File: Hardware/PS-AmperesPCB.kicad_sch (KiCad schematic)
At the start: 10 parts, among them J1 PeripheralCAN, J2 PeripheralCAN

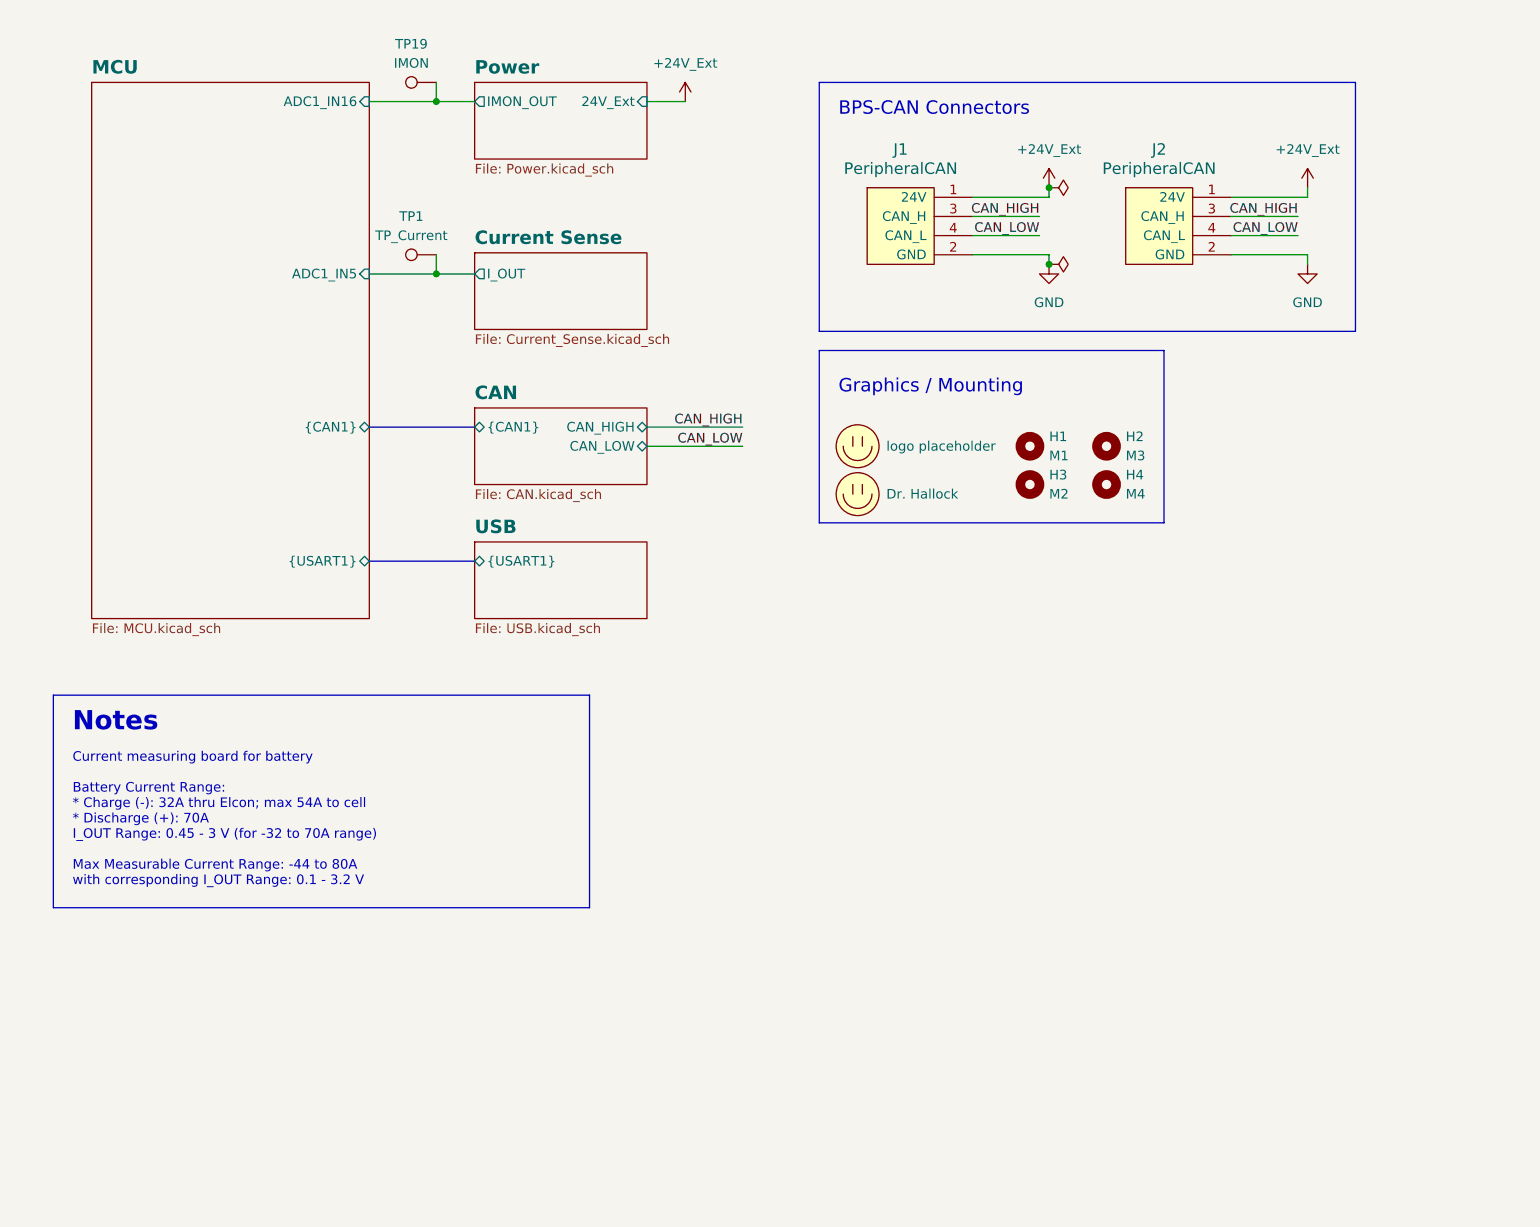
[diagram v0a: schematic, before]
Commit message: added documentation for current range; added VBUS led
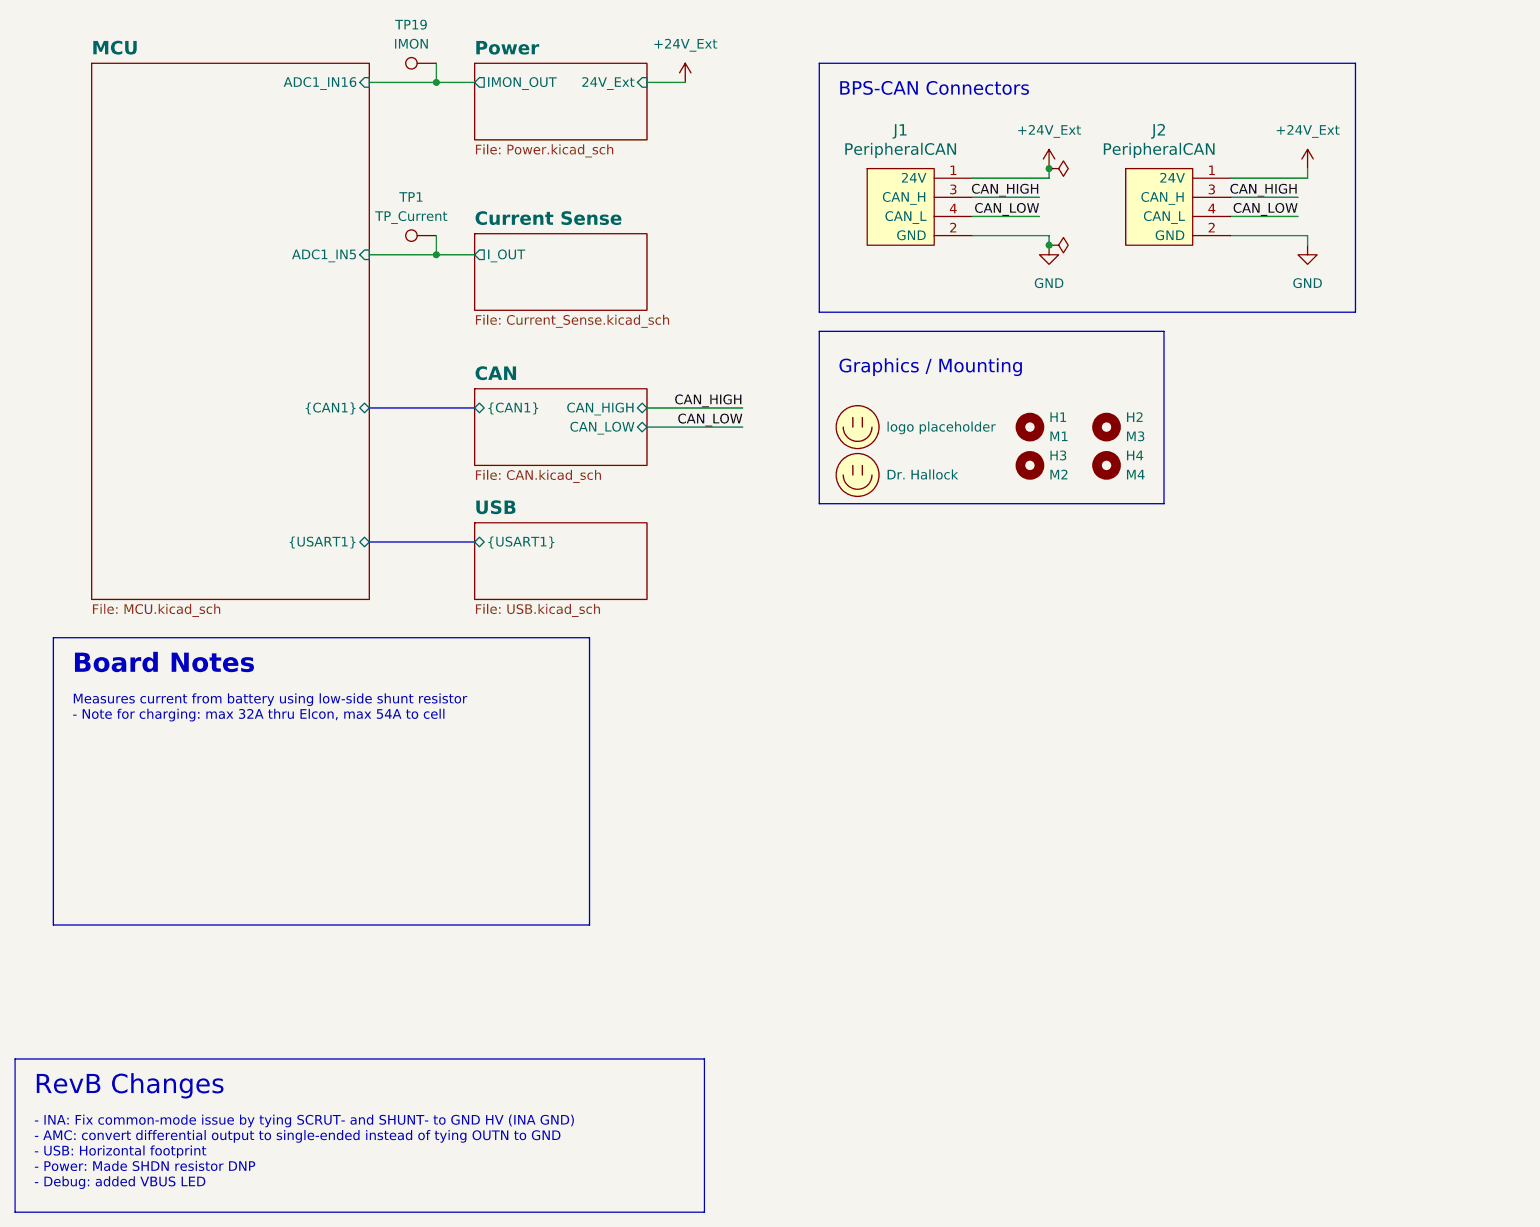
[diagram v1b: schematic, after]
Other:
- note added: "- INA: Fix common-mode issue by tying SCRUT- and SHUNT- to GND HV (INA GND) - AMC: convert differential output to single-ended instead of tying OUTN to GND - USB: Horizontal footprint - Power: Made SHDN resistor DNP - Debug: added VBUS LED"
- note added: "Board Notes"
- note added: "Measures current from battery using low-side shunt resistor - Note for charging: max 32A thru Elcon, max 54A to cell"
- note added: "RevB Changes"
- note removed: "Current measuring board for battery Battery Current Range: * Charge (-): 32A thru Elcon; max 54A to cell * Discharge (+): 70A I_OUT Range: 0.45 - 3 V (for -32 to 70A range) Max Measurable Current Range: -44 to 80A with corresponding I_OUT Range: 0.1 - 3.2 V"
- note removed: "Notes"
- moved on the sheet: H1, H2, H3, H4, J1, J2, TP1, TP19

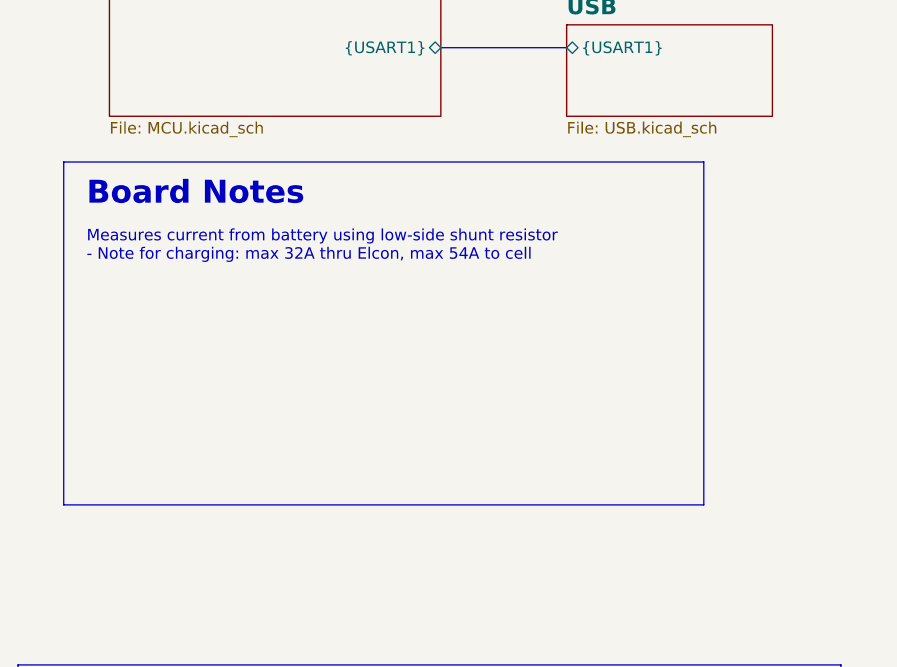
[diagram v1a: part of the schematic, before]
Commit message: INA common-mode fixed (i think)
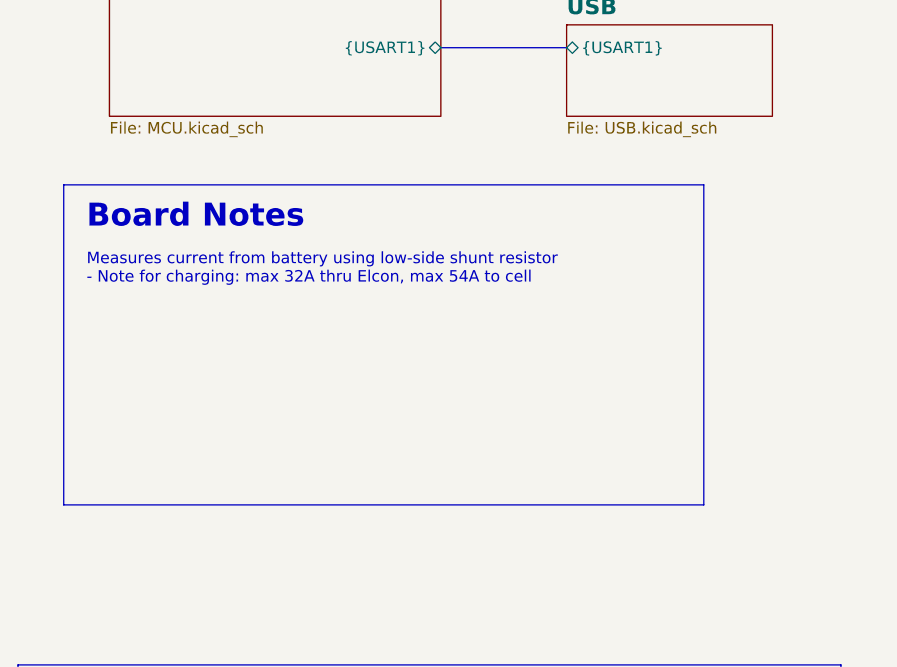
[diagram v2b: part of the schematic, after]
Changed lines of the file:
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@@
 	(paper "A5")
 	(rectangle
-		(start 15.24 96.52)
+		(start 15.24 99.06)
 		(end 86.36 134.62)
 		(stroke
@@
 	(text "Board Notes"
 		(exclude_from_sim no)
-		(at 17.78 101.6 0)
+		(at 17.78 104.14 0)
 		(effects
 			(font
@@
 	(text "Measures current from battery using low-side shunt resistor\n- Note for charging: max 32A thru Elcon, max 54A to cell\n"
 		(exclude_from_sim no)
-		(at 17.78 104.14 0)
+		(at 17.78 106.68 0)
 		(effects
 			(font
@@
 			(table_cell "Measurable Current Range"
 				(exclude_from_sim no)
-				(at 17.78 121.92 0)
+				(at 17.78 122.936 0)
 				(size 27.94 3.048)
 				(margins 0.9525 0.9525 0.9525 0.9525)
@@
 			(table_cell "Current (A)"
 				(exclude_from_sim no)
-				(at 45.72 121.92 0)
+				(at 45.72 122.936 0)
 				(size 15.24 3.048)
 				(margins 0.9525 0.9525 0.9525 0.9525)
@@
 			(table_cell "I_OUT Reading (V)"
 				(exclude_from_sim no)
-				(at 60.96 121.92 0)
+				(at 60.96 122.936 0)
 				(size 20.32 3.048)
 				(margins 0.9525 0.9525 0.9525 0.9525)
@@
 			(table_cell "Max Charge (-)"
 				(exclude_from_sim no)
-				(at 17.78 124.968 0)
+				(at 17.78 125.984 0)
 				(size 27.94 3.048)
 				(margins 0.9525 0.9525 0.9525 0.9525)
@@
 			(table_cell "-46 A"
 				(exclude_from_sim no)
-				(at 45.72 124.968 0)
+				(at 45.72 125.984 0)
 				(size 15.24 3.048)
 				(margins 0.9525 0.9525 0.9525 0.9525)
@@
 			(table_cell "0.1 V"
 				(exclude_from_sim no)
-				(at 60.96 124.968 0)
+				(at 60.96 125.984 0)
 				(size 20.32 3.048)
 				(margins 0.9525 0.9525 0.9525 0.9525)
@@
 			(table_cell "Max Discharge (+)"
 				(exclude_from_sim no)
-				(at 17.78 128.016 0)
+				(at 17.78 129.032 0)
 				(size 27.94 3.048)
 				(margins 0.9525 0.9525 0.9525 0.9525)
@@
 			(table_cell "+78 A"
 				(exclude_from_sim no)
-				(at 45.72 128.016 0)
+				(at 45.72 129.032 0)
 				(size 15.24 3.048)
 				(margins 0.9525 0.9525 0.9525 0.9525)
@@
 			(table_cell "3.2 V"
 				(exclude_from_sim no)
-				(at 60.96 128.016 0)
+				(at 60.96 129.032 0)
 				(size 20.32 3.048)
 				(margins 0.9525 0.9525 0.9525 0.9525)
@@
 			(table_cell "Battery Current Range"
 				(exclude_from_sim no)
-				(at 17.78 109.22 0)
+				(at 17.78 111.76 0)
 				(size 27.94 3.048)
 				(margins 0.9525 0.9525 0.9525 0.9525)
@@
 			(table_cell "Current (A)"
 				(exclude_from_sim no)
-				(at 45.72 109.22 0)
+				(at 45.72 111.76 0)
 				(size 15.24 3.048)
 				(margins 0.9525 0.9525 0.9525 0.9525)
@@
 			(table_cell "I_OUT Reading (V)"
 				(exclude_from_sim no)
-				(at 60.96 109.22 0)
+				(at 60.96 111.76 0)
 				(size 20.32 3.048)
 				(margins 0.9525 0.9525 0.9525 0.9525)
@@
 			(table_cell "Max Charge (-)"
 				(exclude_from_sim no)
-				(at 17.78 112.268 0)
+				(at 17.78 114.808 0)
 				(size 27.94 3.048)
 				(margins 0.9525 0.9525 0.9525 0.9525)
@@
 			(table_cell "-32 A"
 				(exclude_from_sim no)
-				(at 45.72 112.268 0)
+				(at 45.72 114.808 0)
 				(size 15.24 3.048)
 				(margins 0.9525 0.9525 0.9525 0.9525)
@@
 			(table_cell "0.45 V"
 				(exclude_from_sim no)
-				(at 60.96 112.268 0)
+				(at 60.96 114.808 0)
 				(size 20.32 3.048)
 				(margins 0.9525 0.9525 0.9525 0.9525)
@@
 			(table_cell "Max Discharge (+)"
 				(exclude_from_sim no)
-				(at 17.78 115.316 0)
+				(at 17.78 117.856 0)
 				(size 27.94 3.048)
 				(margins 0.9525 0.9525 0.9525 0.9525)
@@
 			(table_cell "+70 A"
 				(exclude_from_sim no)
-				(at 45.72 115.316 0)
+				(at 45.72 117.856 0)
 				(size 15.24 3.048)
 				(margins 0.9525 0.9525 0.9525 0.9525)
@@
 			(table_cell "3.0 V"
 				(exclude_from_sim no)
-				(at 60.96 115.316 0)
+				(at 60.96 117.856 0)
 				(size 20.32 3.048)
 				(margins 0.9525 0.9525 0.9525 0.9525)

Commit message: diff amp / LPF
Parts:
- TP1: value TP_Current -> I_OUT
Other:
- note added: "RevB Changelog"
- note removed: "RevB Changes"
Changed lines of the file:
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@@
 	)
 	(rectangle
-		(start 10.16 152.4)
-		(end 101.6 172.72)
+		(start 104.394 82.55)
+		(end 195.834 102.87)
 		(stroke
 			(width 0)
@@
 		)
 	)
-	(text "RevB Changes"
-		(exclude_from_sim no)
-		(at 12.7 157.48 0)
+	(text "RevB Changelog"
+		(exclude_from_sim no)
+		(at 106.934 87.63 0)
 		(effects
 			(font
@@
 	(text "- INA: Fix common-mode issue by tying SCRUT- and SHUNT- to GND HV (INA GND)\n- AMC: convert differential output to single-ended instead of tying OUTN to GND\n- USB: Horizontal footprint\n- Power: Made SHDN resistor DNP\n- Debug: added VBUS LED"
 		(exclude_from_sim no)
-		(at 12.7 160.02 0)
+		(at 106.934 90.17 0)
 		(effects
 			(font
@@
 			)
 		)
-		(property "Value" "TP_Current"
+		(property "Value" "I_OUT"
 			(at 62.738 40.64 90)
 			(effects

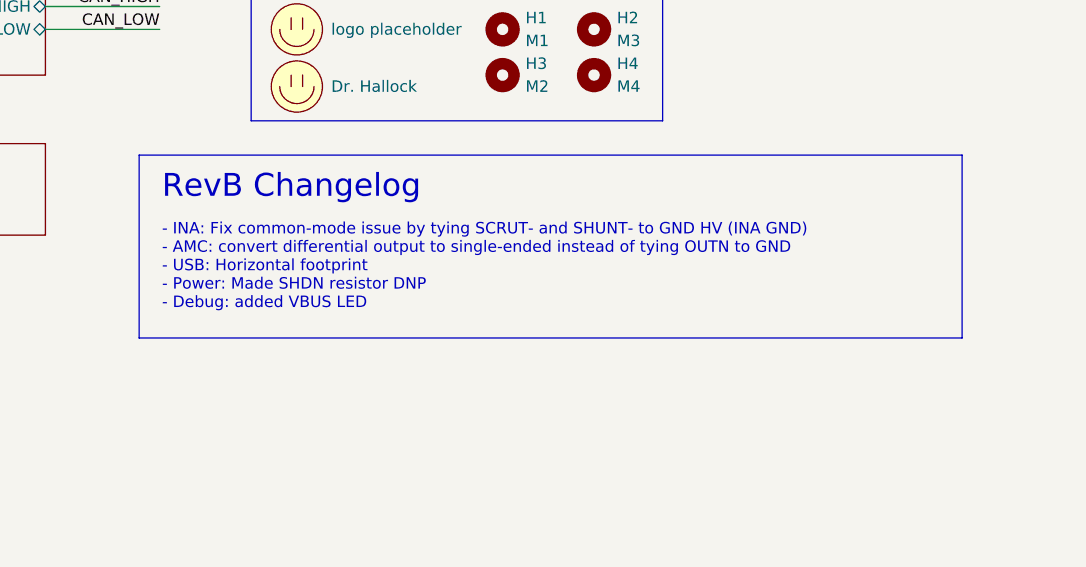
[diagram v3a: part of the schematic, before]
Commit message: new TLV symbol, SPDT switch for scrut
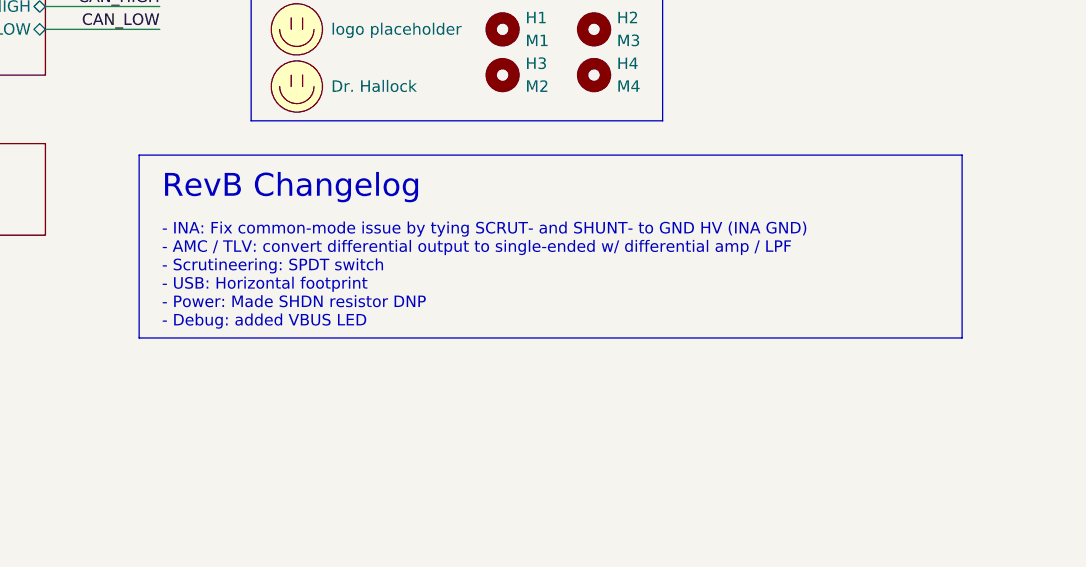
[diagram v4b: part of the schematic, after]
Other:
- note added: "- INA: Fix common-mode issue by tying SCRUT- and SHUNT- to GND HV (INA GND) - AMC / TLV: convert differential output to single-ended w/ differential amp / LPF - Scrutineering: SPDT switch - USB: Horizontal footprint - Power: Made SHDN resistor DNP - Debug: added VBUS LED"
- note removed: "- INA: Fix common-mode issue by tying SCRUT- and SHUNT- to GND HV (INA GND) - AMC: convert differential output to single-ended instead of tying OUTN to GND - USB: Horizontal footprint - Power: Made SHDN resistor DNP - Debug: added VBUS LED"
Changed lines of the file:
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@@
 		)
 	)
-	(text "- INA: Fix common-mode issue by tying SCRUT- and SHUNT- to GND HV (INA GND)\n- AMC: convert differential output to single-ended instead of tying OUTN to GND\n- USB: Horizontal footprint\n- Power: Made SHDN resistor DNP\n- Debug: added VBUS LED"
+	(text "- INA: Fix common-mode issue by tying SCRUT- and SHUNT- to GND HV (INA GND)\n- AMC / TLV: convert differential output to single-ended w/ differential amp / LPF\n- Scrutineering: SPDT switch\n- USB: Horizontal footprint\n- Power: Made SHDN resistor DNP\n- Debug: added VBUS LED"
 		(exclude_from_sim no)
 		(at 106.934 90.17 0)
